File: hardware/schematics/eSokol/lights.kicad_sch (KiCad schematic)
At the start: 29 parts, among them Q1 AO3400A, Q2 AO3400A, Q3 AO3400A, Q7 AO3401A, SW5 EMERG_BULBS, U1 hw-045 20V step-up

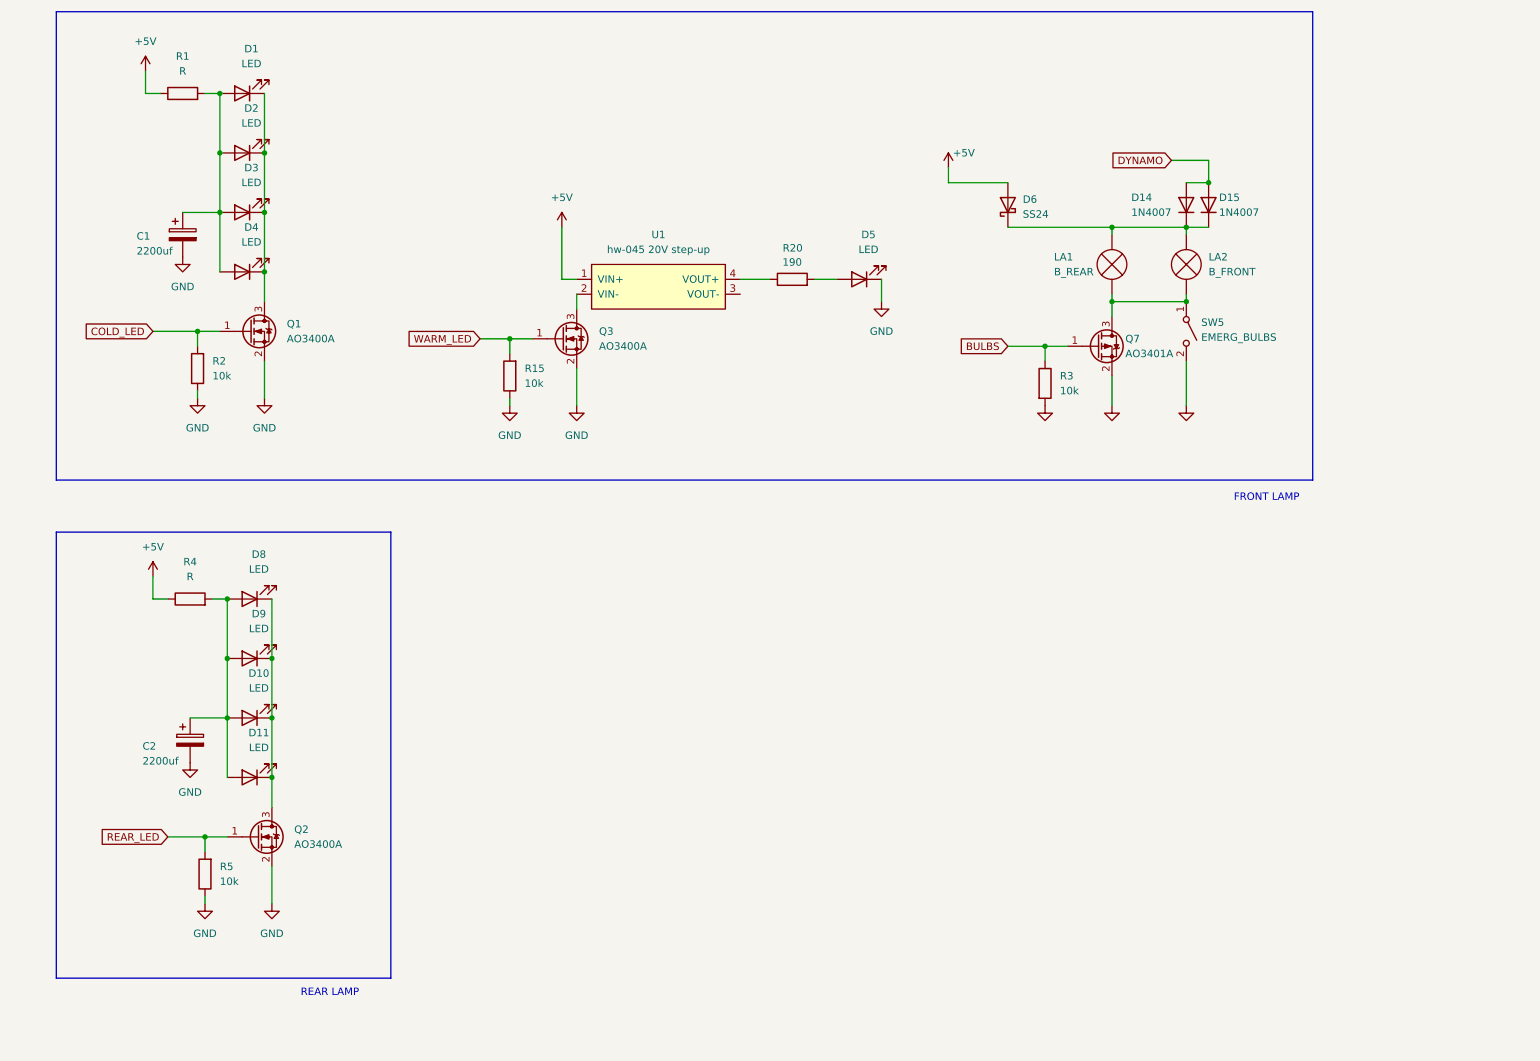
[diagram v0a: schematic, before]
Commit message: Minor lights fixes and improvements, added decoupling cap to mcu 5V, removed unused files
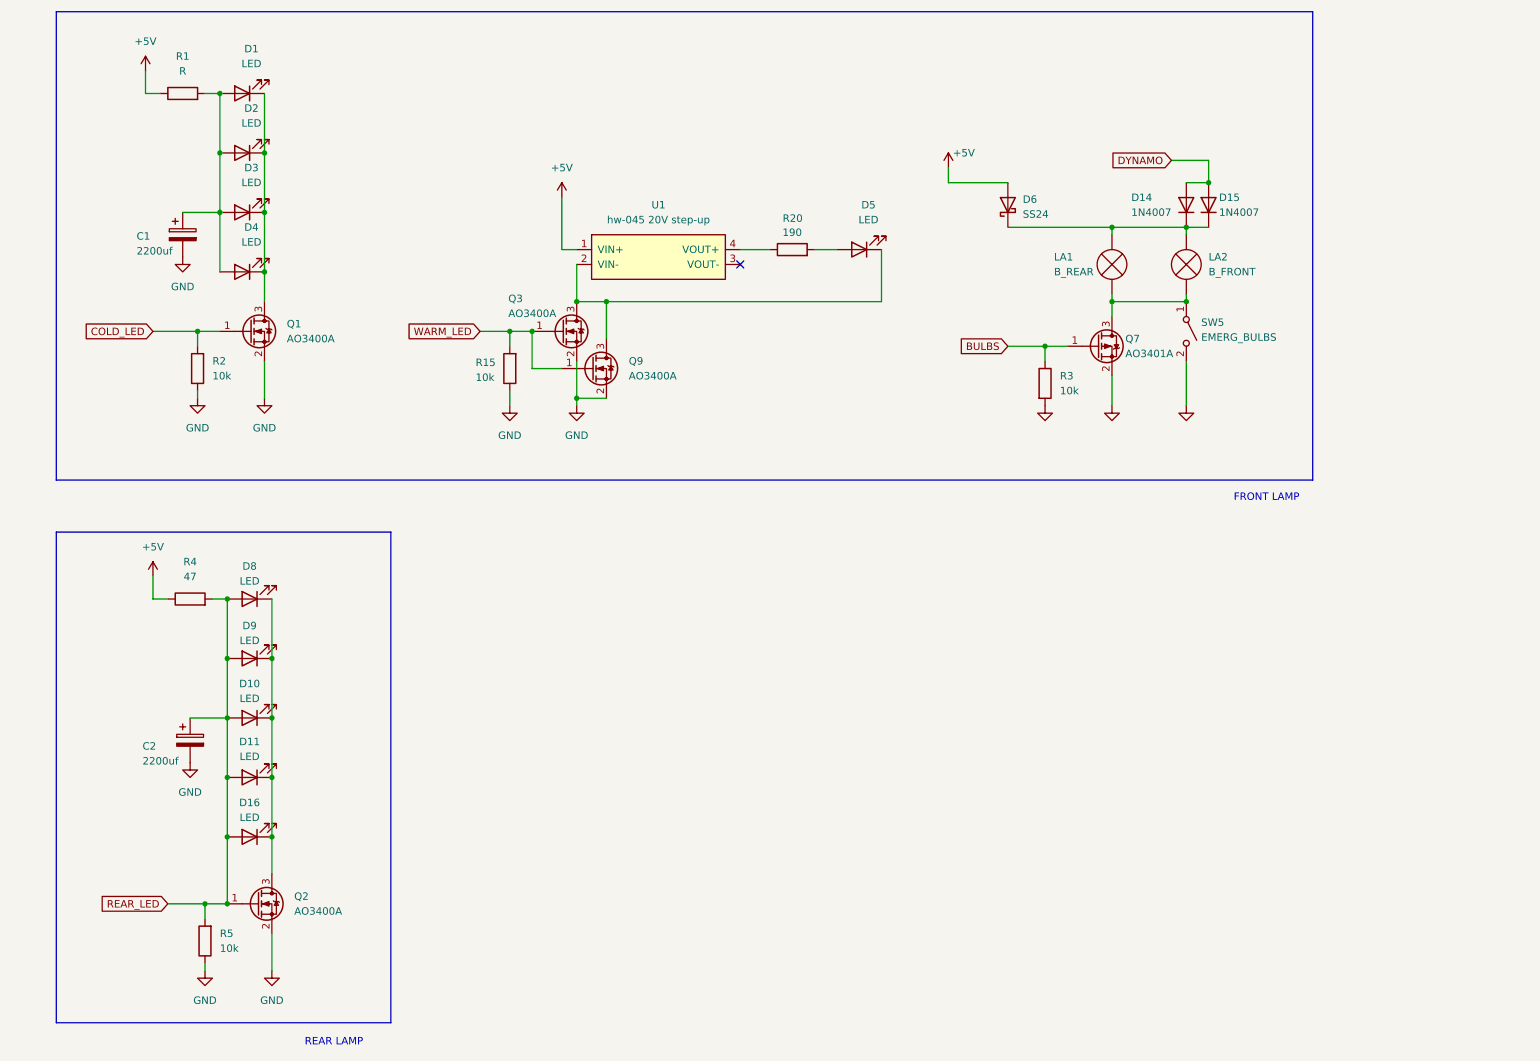
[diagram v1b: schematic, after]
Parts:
- added D16: LED, symbol Device:LED
- added Q9: AO3400A, Package_TO_SOT_SMD:SOT-23, symbol Transistor_FET:AO3400A
- R4: value R -> 47
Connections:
- net GND: now also Q9.2 (S); no longer D5.1 (K)
- net REAR_LED: now also C2.1, D10.2 (A), D11.2 (A), D8.2 (A), D9.2 (A), R4.2, D16.2 (A)
- net WARM_LED: now also Q9.1 (G)
- net at Q3.3 (D), U1.2 (VIN-): now also D5.1 (K), Q9.3 (D)
- net at D10.1 (K), D11.1 (K), D8.1 (K)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: now also D16.1 (K)
- no-connect marks 0 -> 1
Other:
- moved on the sheet: D5, Q2, Q3, R15, R20, R5, U1

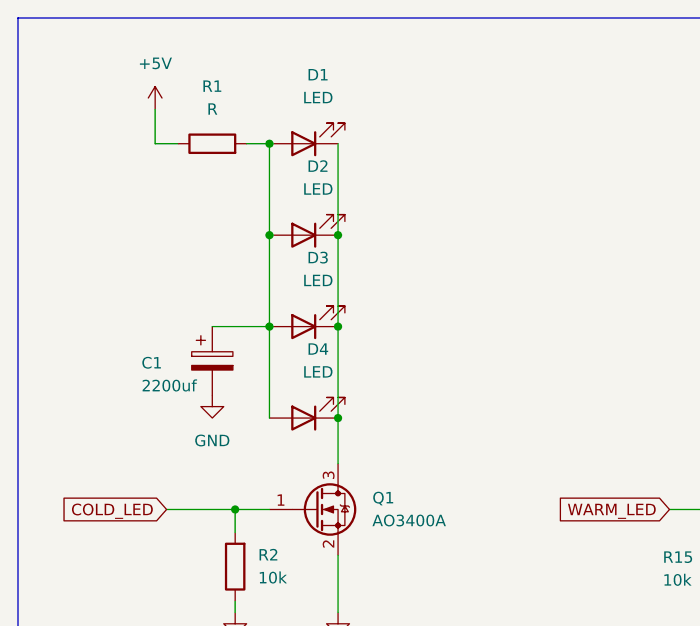
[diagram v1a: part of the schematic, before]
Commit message: hardware/schematics: Replace screen-based control for HC-05 smartphone-app-based control, add buzzer RC filter, rework cold LED circuit
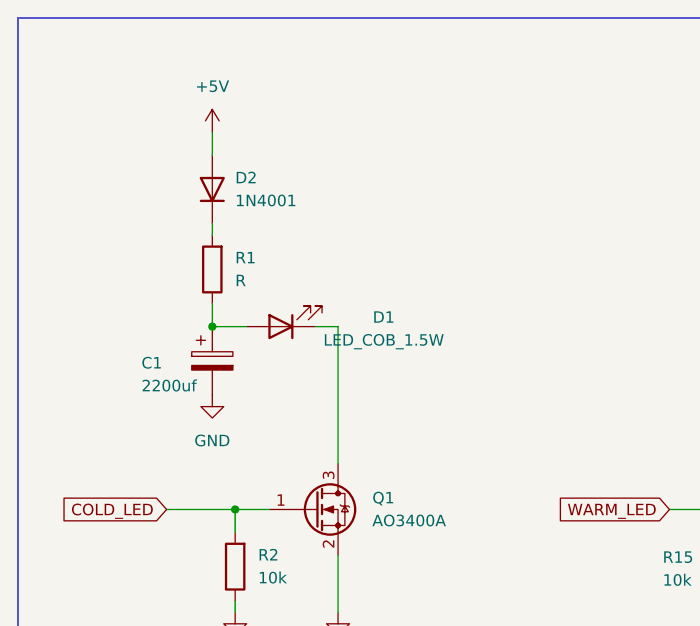
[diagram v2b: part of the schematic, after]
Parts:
- removed D2, D3, D4: LED, symbol Device:LED
- added D2: 1N4001, Diode_THT:D_DO-41_SOD81_P10.16mm_Horizontal, symbol Diode:1N4001
- D1: value LED -> LED_COB_1.5W
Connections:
- net +5V: now also D2.2 (A); no longer R1.1
- net at C1.1, D1.2 (A): now also R1.1; no longer R1.2
- new net: D2.1 (K), R1.2
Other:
- moved on the sheet: D1, R1

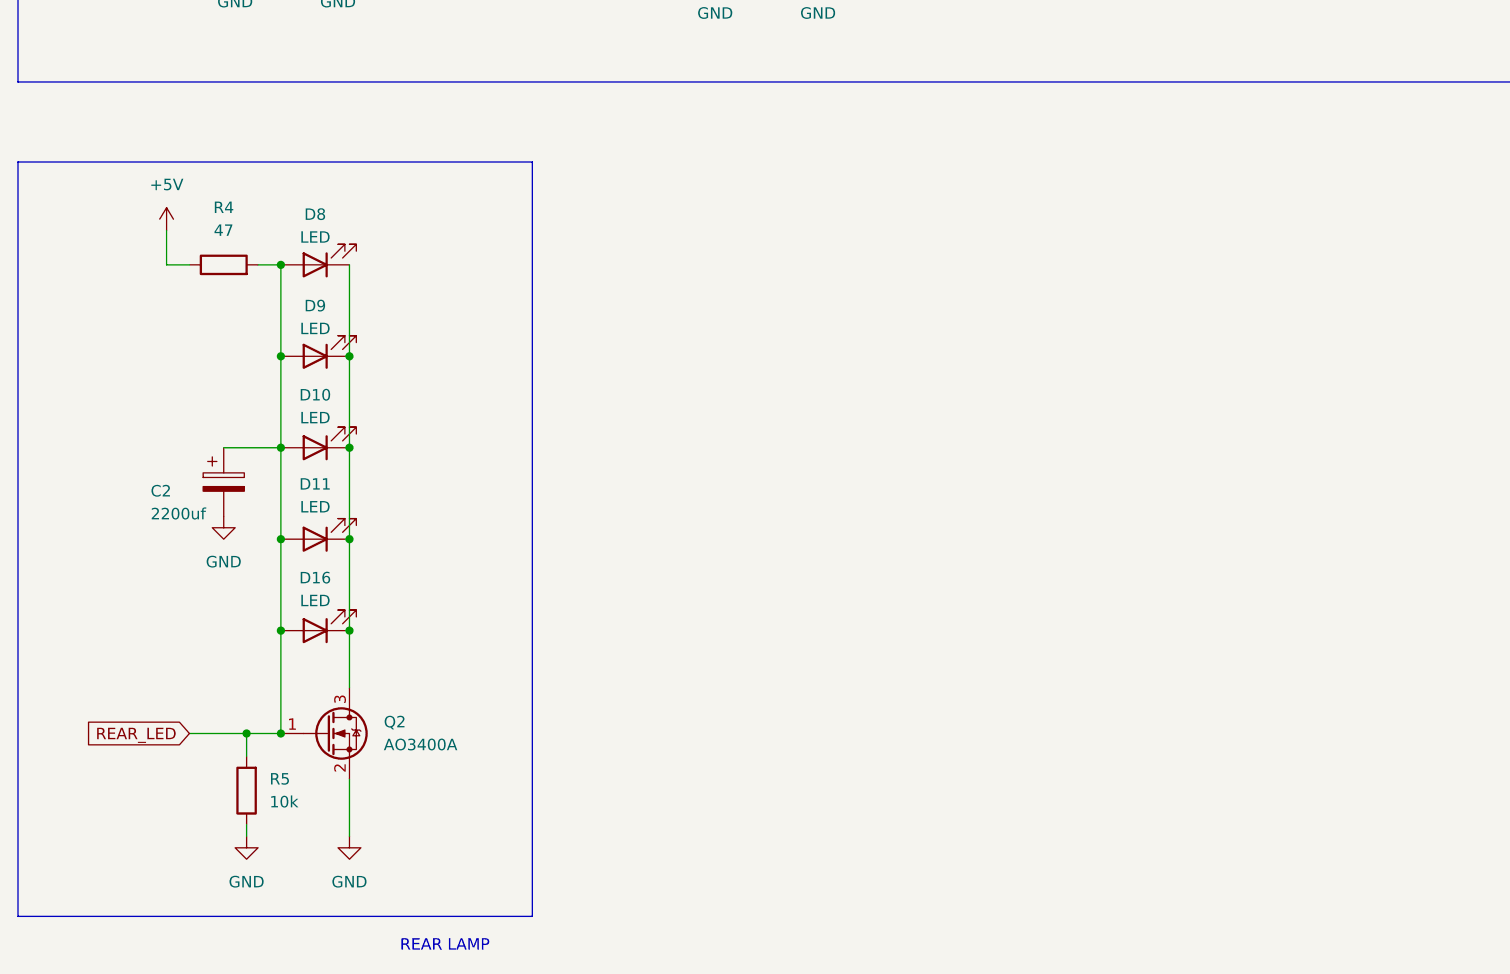
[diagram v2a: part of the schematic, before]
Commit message: hardware/schematics: add initial blinkers and brake handler circuits
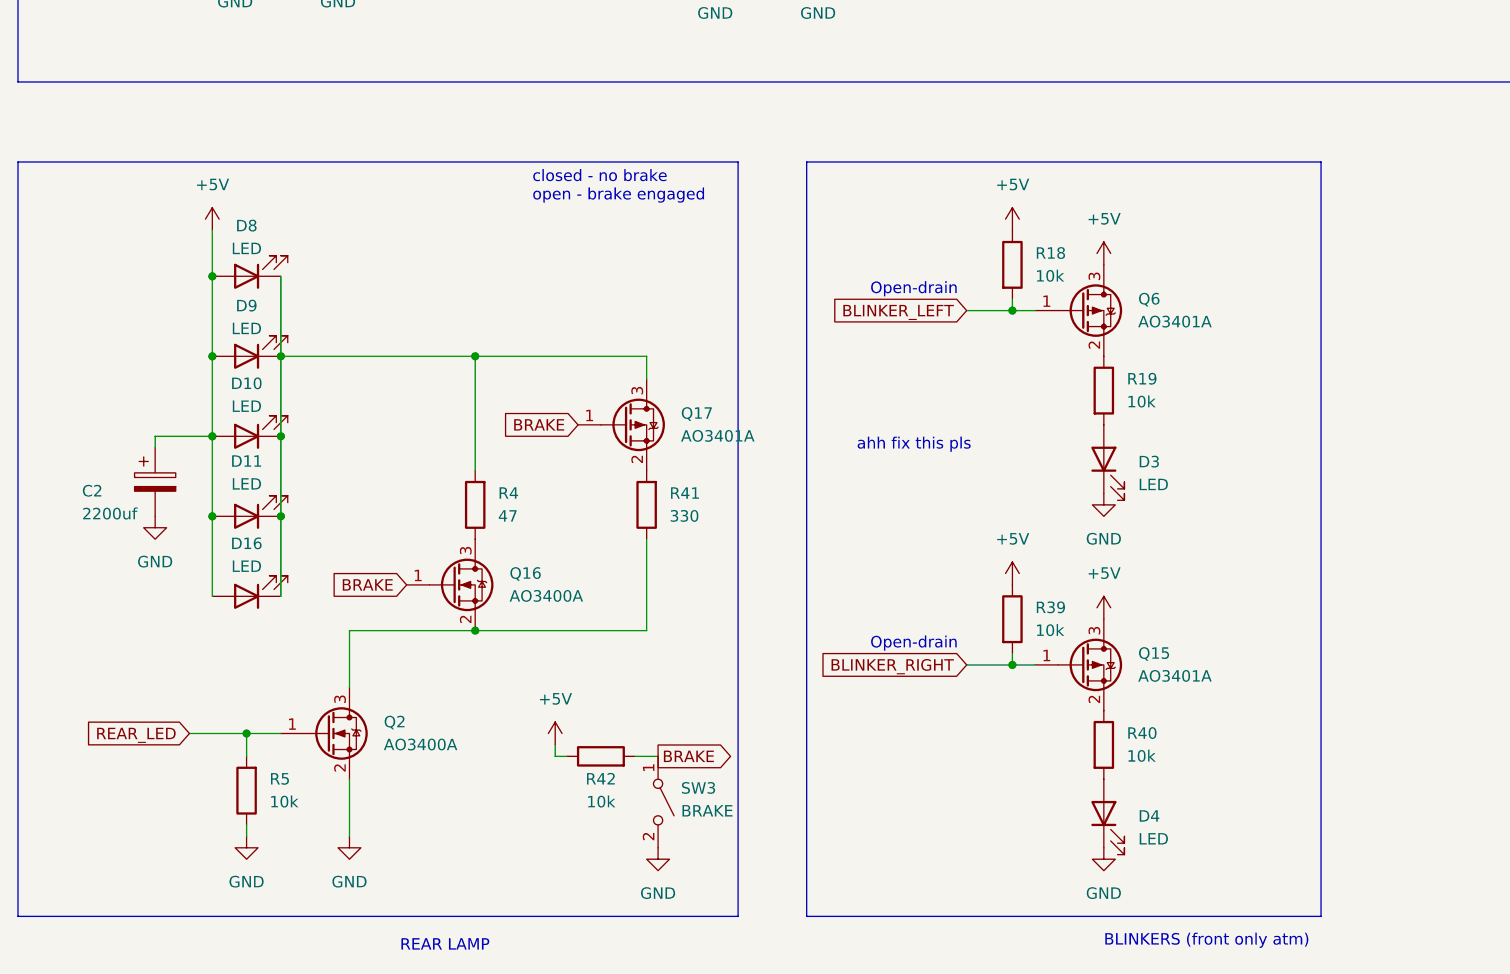
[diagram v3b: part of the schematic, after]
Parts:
- added D3, D4: LED, symbol Device:LED
- added Q15, Q17, Q6: AO3401A, Package_TO_SOT_SMD:SOT-23, symbol Transistor_FET:AO3401A
- added Q16: AO3400A, Package_TO_SOT_SMD:SOT-23, symbol Transistor_FET:AO3400A
- added R18, R19, R39, R40, R42: 10k, symbol Device:R
- added R41: 330, symbol Device:R
- added SW3: BRAKE, symbol Switch:SW_SPST
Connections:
- net +5V: now also C2.1, D10.2 (A), D11.2 (A), D16.2 (A), D8.2 (A), D9.2 (A), Q15.3 (D), Q6.3 (D), R18.1, R39.1, R42.1; no longer R4.1
- net GND: now also D3.1 (K), D4.1 (K), SW3.2 (B)
- net REAR_LED: no longer C2.1, D10.2 (A), D11.2 (A), D16.2 (A), D8.2 (A), D9.2 (A), R4.2
- net at D10.1 (K), D11.1 (K), D16.1 (K)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: now also R4.2, Q17.3 (D); no longer Q2.3 (D)
- new net: Q17.2 (S), R41.2
- new net: Q16.2 (S), Q2.3 (D), R41.1
- new net: Q16.3 (D), R4.1
- new net: Q15.2 (S), R40.1
- new net: Q6.2 (S), R19.1
- new net: D4.2 (A), R40.2
- new net: D3.2 (A), R19.2
- new net BLINKER_LEFT: Q6.1 (G), R18.2
- new net BLINKER_RIGHT: Q15.1 (G), R39.2
- new net BRAKE: Q16.1 (G), Q17.1 (G), R42.2, SW3.1 (A)
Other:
- note added: "BLINKERS (front only atm)"
- note added: "Open-drain"
- note added: "ahh fix this pls"
- note added: "closed - no brake open - brake engaged"
- moved on the sheet: C2, D10, D11, D16, D8, D9

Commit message: hardware/schematics: finish-ify blinkers circuit, mark old blinkers circuit as outdated
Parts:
- R19, R40: value 10k -> 150
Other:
- note added: "closed - no brake light dim open - brake engaged light bright"
- note removed: "closed - no brake open - brake engaged"
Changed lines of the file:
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@@
 		)
 	)
-	(text "closed - no brake\nopen - brake engaged"
+	(text "closed - no brake light dim\nopen - brake engaged light bright"
 		(exclude_from_sim no)
-		(at 85.09 108.204 0)
+		(at 82.804 108.712 0)
 		(effects
 			(font
@@
 			)
 		)
-		(property "Value" "10k"
+		(property "Value" "150"
 			(at 151.13 171.4499 0)
 			(effects
@@
 			)
 		)
-		(property "Value" "10k"
+		(property "Value" "150"
 			(at 151.13 132.0799 0)
 			(effects

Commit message: hardware/schematics: updated eSokol to reflect new features: ambient light LDR sensor and blinkers Remove old NE555-based blinkers circuit too
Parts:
- added D12, D26: LED, symbol Device:LED
- added R43, R44: 150, symbol Device:R
- added SW4: SW_BLINKERS, symbol Switch:SW_SPDT_MSM
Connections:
- net GND: now also D12.1 (K), D26.1 (K)
- net at Q15.2 (S), R40.1: now also R43.1
- net at Q6.2 (S), R19.1: now also R44.1
- new net: D26.2 (A), R44.2
- new net: D12.2 (A), R43.2
- new net +3V3: SW4.2 (3)
- new net BLINKER_LEFT_IN: SW4.1
- new net BLINKER_RIGHT_IN: SW4.3 (4)
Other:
- note added: "BLINKERS"
- note removed: "BLINKERS (front only atm)"
- moved on the sheet: C2, D10, D11, D16, D8, D9, Q16, Q17, Q2, R4, R41, R42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

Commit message: WIP: update some schematics to reflect the newest design changes
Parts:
- removed D12: LED, symbol Device:LED
- removed Q15: AO3401A, Package_TO_SOT_SMD:SOT-23, symbol Transistor_FET:AO3401A
- removed R39: 10k, symbol Device:R
- removed R40, R43: 150, symbol Device:R
- added D27: LED, symbol Device:LED
- added Q10, Q11, Q8: AO3401A, Package_TO_SOT_SMD:SOT-23, symbol Transistor_FET:AO3401A
- added R21, R22, R23: 10k, symbol Device:R
- added R24, R47: 150, symbol Device:R
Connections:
- net +5V: now also Q10.3 (D), Q11.3 (D), Q8.3 (D), R21.1, R22.1, R23.1
- net BLINKER_LEFT: now also Q8.1 (G), R21.2
- net BLINKER_RIGHT: now also Q10.1 (G), Q11.1 (G), R22.2, R23.2
- net GND: now also R44.2, R47.2; no longer D26.1 (K)
- net at Q6.2 (S), R19.1: no longer R44.1
- net at D4.2 (A): now also R24.2
- net at D26.2 (A): now also Q8.2 (S); no longer R44.2
- new net: Q10.2 (S), R24.1
- new net: D27.1 (K), R47.1
- new net: D27.2 (A), Q11.2 (S)
- new net: D26.1 (K), R44.1
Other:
- moved on the sheet: D26, D3, Q6, R18, R19, R44, SW4
